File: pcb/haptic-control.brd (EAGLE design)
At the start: 40 x 160 mm, 47 parts, among them M1 SPH0641LM4H-1, U1 CC2642R, U2 SST26VF064B, U3 ICM20948, U4 74LVC1G17, U5 MCP1700T-1802TT, U6 PCA9306-DCU, U7 MTCH6301, X1 48MHz, X2 32.768kHz

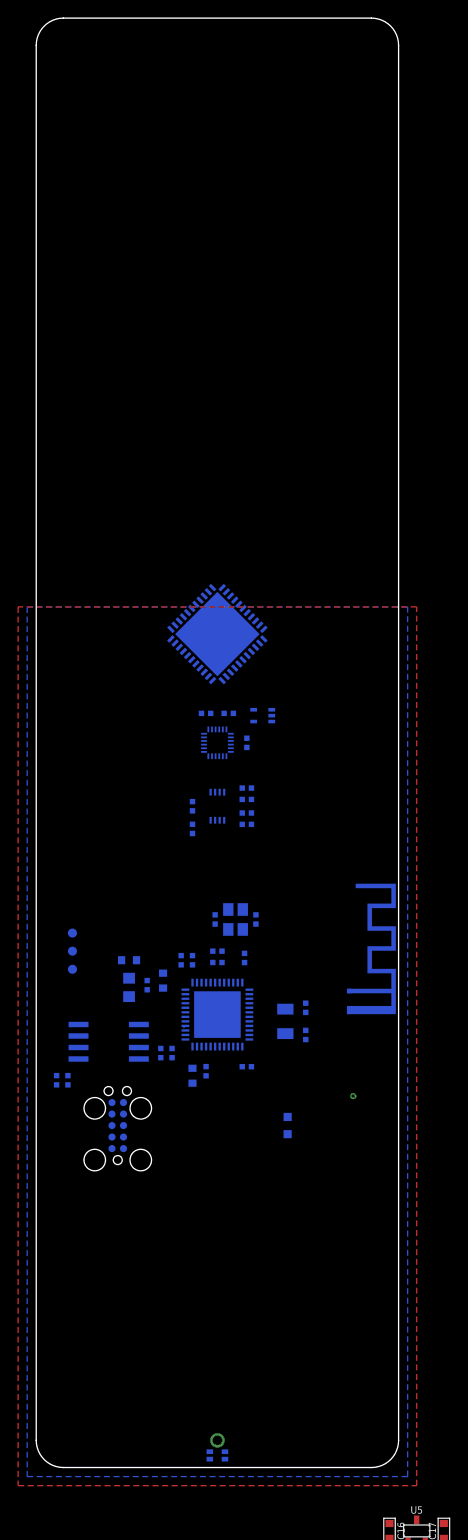
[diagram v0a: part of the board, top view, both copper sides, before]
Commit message: minor sch value modifications, and ic additions; minor pcb constraints changes
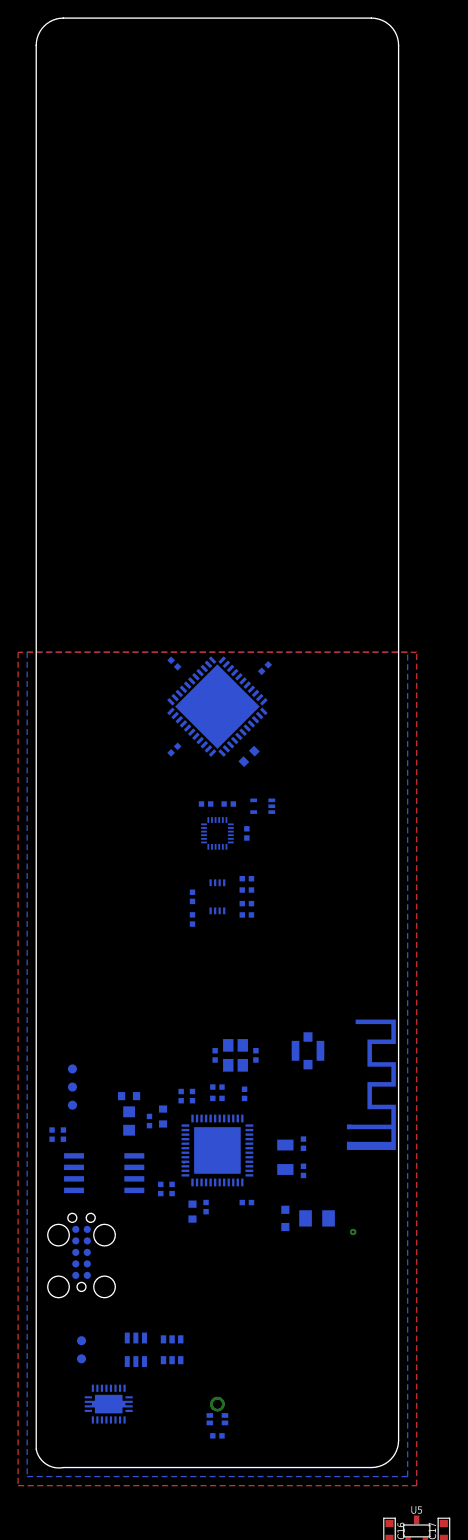
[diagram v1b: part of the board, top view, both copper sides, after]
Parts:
- added A1: U.FL, Connectors > Antennas:U.FL
- added C22, C23, C25, C26: 100n, Passive Components > Capacitors > Multilayer Ceramic Capacitors MLCC:_0402
- added C24: 10u, Passive Components > Capacitors > Multilayer Ceramic Capacitors MLCC:0603_WAVE
- added C27: 100u, Passive Components > Capacitors > Multilayer Ceramic Capacitors MLCC:_1206
- added TP4, TP5: TEST_POINT, Utility > Board:TEST_POINT
- added U$1: FS312F-G, Power > Battery Management:SOT23-6
- added U$2: FS8205, Semiconductors > Discrete Semiconductors > Transistors > MOSFETs:SOT23-6
- added U8: BQ51050B, Texas Instruments:VQFN20
- C10, C9: value 3p -> 12p
- C11, C12: value (none) -> np
- C4: value (none) -> 22u
- C6: value 10u -> 22u
- L1: value 10u -> 6u8
- L2: value filter -> BLM18HE152SN1
- moved C10 15.0 mm to (29.5, 35.8)
- moved C5 15.0 mm to (12.5, 38.2)
- moved C9 15.0 mm to (29.5, 32.8)
- moved C1 15.0 mm to (23.2, 29.2)
- moved C11 15.0 mm to (24.2, 45.5)
- moved C12 15.0 mm to (19.8, 45.5)
- moved C13 15.0 mm to (17.2, 28.2)
- moved C14 15.0 mm to (17.2, 41.0)
- moved C15 15.0 mm to (13.8, 30.8)
- moved C2 15.0 mm to (18.8, 28.8)
- moved C3 15.0 mm to (20.0, 40.8)
- moved C4 15.0 mm to (14.0, 38.8)
- moved C6 15.0 mm to (10.2, 41.0)
- moved C7 15.0 mm to (20.0, 42.0)
- moved C8 15.0 mm to (23.0, 41.2)
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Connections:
- new net N$10: C24.P$1, U7.7
- new net TC_!RESET: U7.18
- new net TC_INT: U7.8
- net 3.3V: now also C22.1, C23.1, C25.1, C26.1, C27.1, U7.17, U7.28, U7.40
- net GND: now also C22.2, C23.2, C24.P$2, C25.2, C26.2, C27.2, U7.16, U7.29, U7.39, U7.45, U7.6
- net SCL: now also U7.44
- net SDA: now also U7.1
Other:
- outline, holes or cut-outs redrawn

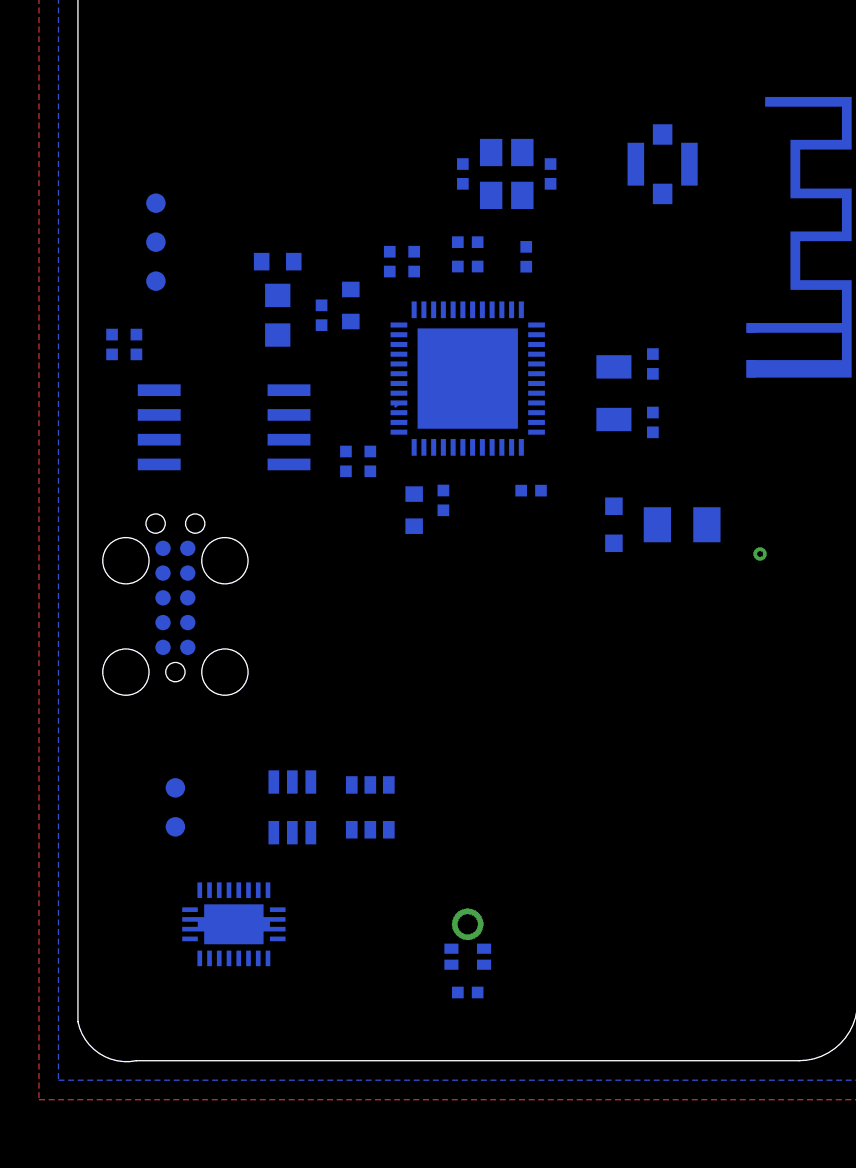
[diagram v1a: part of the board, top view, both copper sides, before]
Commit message: Hand merged previous commits: 	Added CC26x2 reference design 	Added antenna matching 	Connected labels to touch IC 	Added keepouts for the antenna 	Added more references/info to the board and schematic
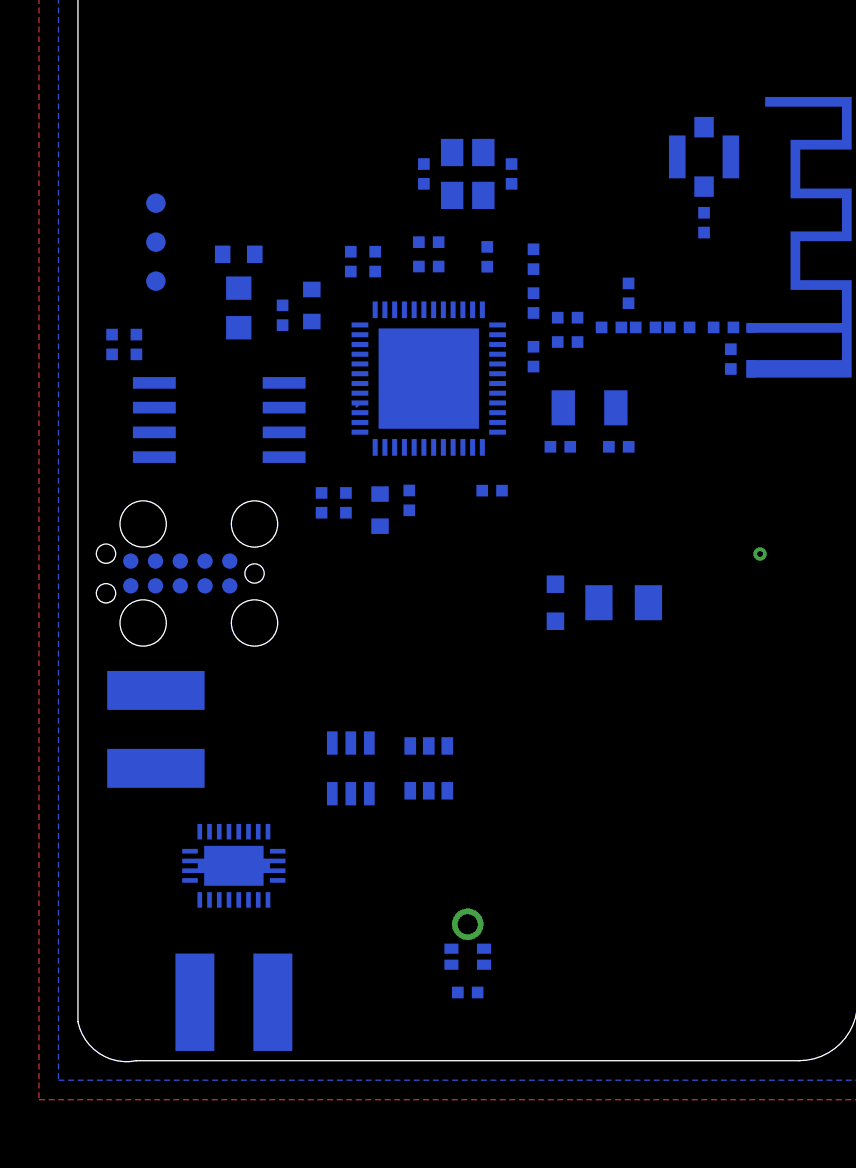
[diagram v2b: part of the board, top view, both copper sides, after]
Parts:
- removed TP4, TP5: TEST_POINT, Utility > Board:TEST_POINT
- added C28, C29, C31: 1p, Passive Components > Capacitors > Multilayer Ceramic Capacitors MLCC:_0402
- added C30, C33: 12p, Passive Components > Capacitors > Multilayer Ceramic Capacitors MLCC:_0402
- added C32: 1p8, Passive Components > Capacitors > Multilayer Ceramic Capacitors MLCC:_0402
- added C34, C35: DNP, Passive Components > Capacitors > Multilayer Ceramic Capacitors MLCC:_0402
- added L3, L4: 2n4, Passive Components > Inductors, Chokes & Coils:_0402
- added L5, L6: 2N, Passive Components > Inductors, Chokes & Coils:_0402
- added P1, P2: 2P-PAD, Generic Connector:PAD2X5MM-2P
- C11, C12: value np -> DNP
- moved C27 5.00 mm to (28.0, 23.5)
- moved L2 5.00 mm to (24.5, 23.5)
- moved C9 4.91 mm to (24.8, 31.5), turned to 0 degrees
- moved C10 4.60 mm to (27.8, 31.5), turned to 0 degrees
- moved U$1 3.61 mm to (14.0, 15.0)
- moved U$2 3.61 mm to (18.0, 15.0)
- moved U8 3.00 mm to (8.00, 10.0)
- moved C15 2.47 mm to (12.5, 28.6)
- moved R5 2.47 mm to (13.8, 28.6)
- moved A1 2.16 mm to (32.1, 46.4), turned to 270 degrees
- moved C6 2.03 mm to (8.25, 41.4)
- moved L1 2.03 mm to (8.25, 38.6)
- moved C1 2.00 mm to (21.2, 29.2)
- moved C11 2.00 mm to (22.2, 45.5)
- moved C12 2.00 mm to (17.8, 45.5)
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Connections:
- new net N$14: C30.1, L3.1
- new net N$15: C29.1, L4.1, L5.2
- new net N$16: C31.1, L5.1, L6.2
- new net N$17: C32.2, C35.1, E1.ANT
- new net N$18: C32.1, C33.2
- new net N$19: C33.1, C34.2, L6.1
- new net N$20: A1.P$3, C34.1
- new net PCAP_RX0: U7.27
- new net PCAP_RX1: U7.26
- new net PCAP_RX10: U7.14
- new net PCAP_RX11: U7.11
- new net PCAP_RX12: U7.10
- new net PCAP_RX2: U7.25
- new net PCAP_RX3: U7.24
- new net PCAP_RX4: U7.23
- new net PCAP_RX5: U7.22
- new net PCAP_RX6: U7.21
- new net PCAP_RX7: U7.20
- new net PCAP_RX8: U7.19
- new net PCAP_RX9: U7.15
- new net PCAP_TX0: U7.33
- new net PCAP_TX1: U7.32
- new net PCAP_TX10: U7.42
- new net PCAP_TX11: U7.43
- new net PCAP_TX12: U7.13
- new net PCAP_TX13: U7.12
- new net PCAP_TX14: U7.5
- new net PCAP_TX15: U7.4
- new net PCAP_TX16: U7.3
- new net PCAP_TX17: U7.2
- new net PCAP_TX2: U7.31
- new net PCAP_TX3: U7.30
- new net PCAP_TX4: U7.34
- new net PCAP_TX5: U7.38
- new net PCAP_TX6: U7.37
- new net PCAP_TX7: U7.36
- new net PCAP_TX8: U7.35
- new net PCAP_TX9: U7.41
- net GND: now also A1.P$1, A1.P$2, C28.1, C30.2, C31.2, C35.2, E1.GND
- net N$1: now also C28.2, L4.2
- net N$3: now also C29.2, L3.2

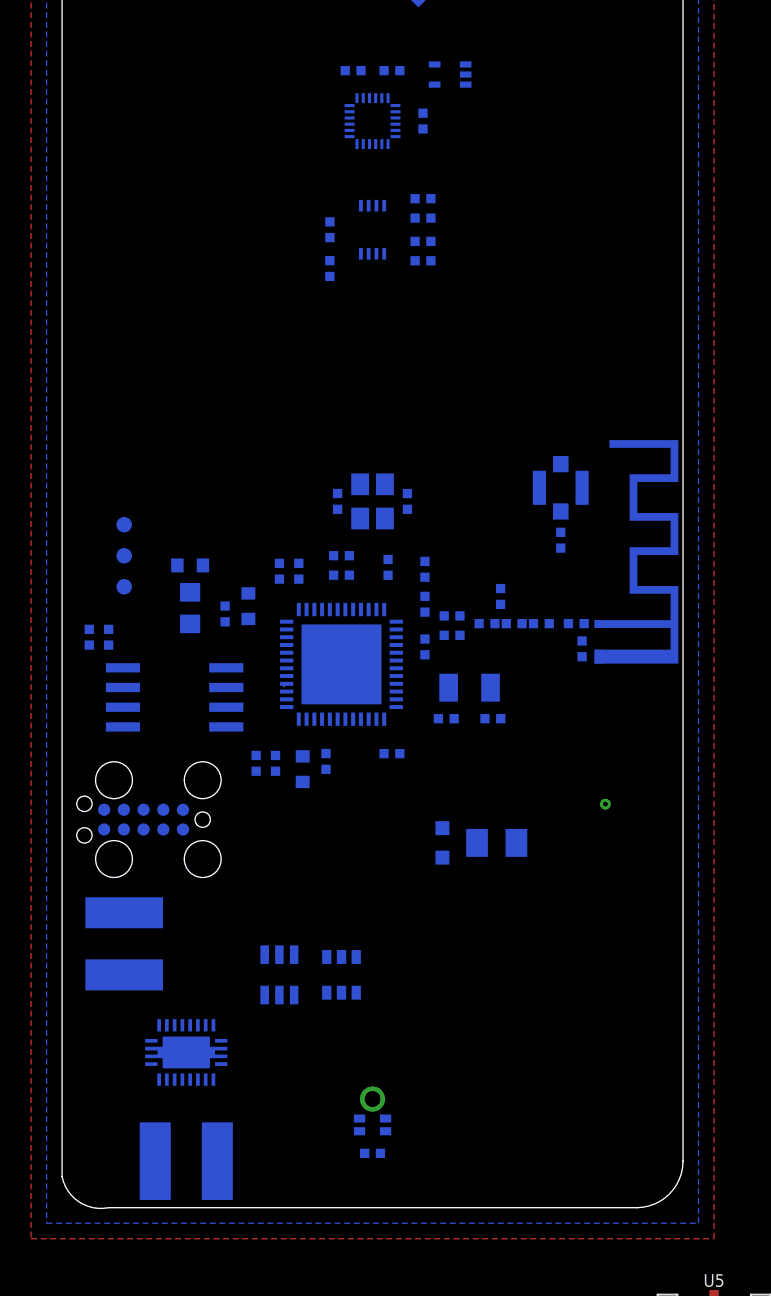
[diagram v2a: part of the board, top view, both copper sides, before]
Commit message: added battery and coil pads, changed mcu orientation
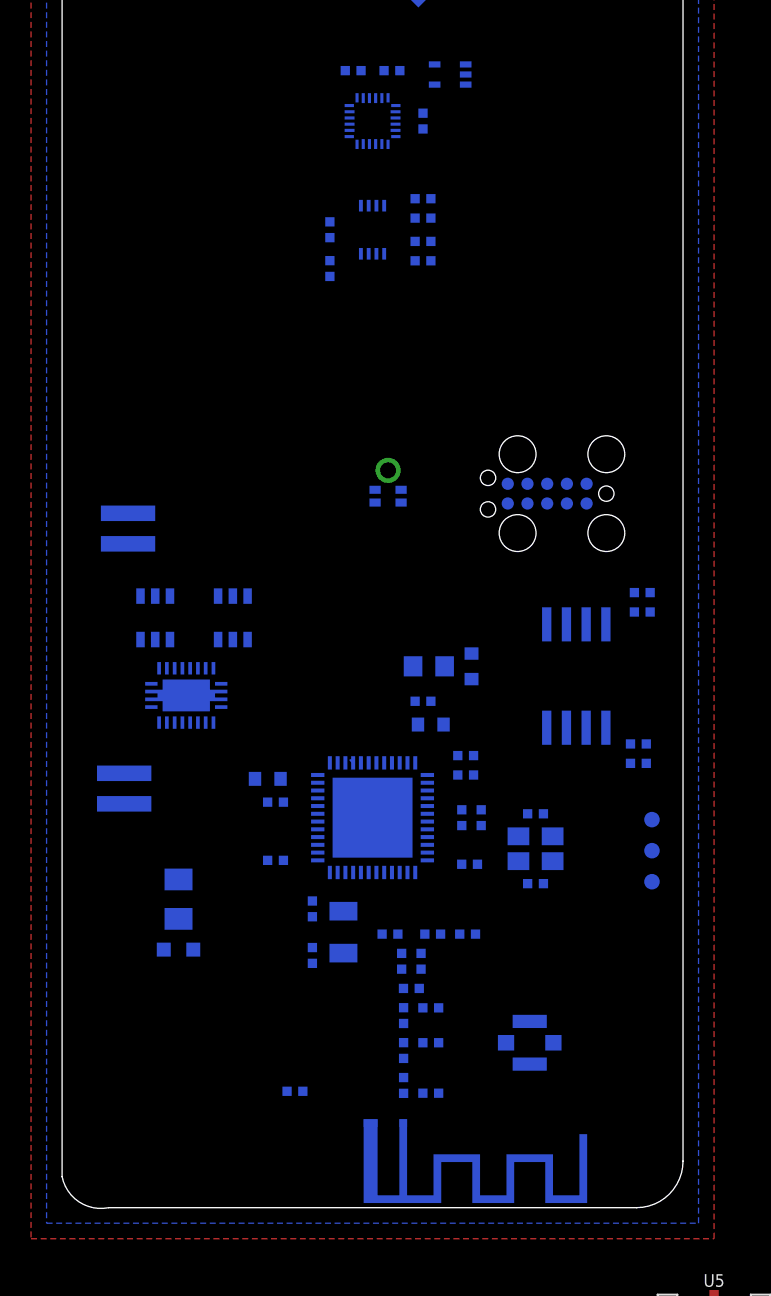
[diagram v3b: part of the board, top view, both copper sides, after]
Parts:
- removed P1, P2: 2P-PAD, Generic Connector:PAD2X5MM-2P
- removed U$1: FS312F-G, Power > Battery Management:SOT23-6
- removed U$2: FS8205, Semiconductors > Discrete Semiconductors > Transistors > MOSFETs:SOT23-6
- added J1, J2: PAD1X3_5MM-2P, Connectors > Other:PAD1X3_5MM-2P
- added U10: FS8205, Fortune:SOT23-6
- added U9: FS312F-G, Fortune:SOT23-6
- moved TP1 41.0 mm to (38.0, 21.0), turned to 180 degrees
- moved M1 40.5 mm to (21.0, 47.5)
- moved TP2 38.9 mm to (38.0, 23.0), turned to 180 degrees
- moved TP3 37.2 mm to (38.0, 25.0), turned to 180 degrees
- moved R2 36.0 mm to (37.1, 29.9), turned to 180 degrees
- moved A1 35.8 mm to (30.1, 10.6), turned to 0 degrees
- moved R4 35.1 mm to (37.1, 28.6), turned to 180 degrees
- moved E1 34.8 mm to (22.0, 5.20), turned to 180 degrees
- moved C34 33.4 mm to (23.8, 10.6), turned to 0 degrees
- moved TC1 33.4 mm to (31.2, 46.0)
- moved C32 31.8 mm to (22.0, 7.88), turned to 270 degrees
- moved C35 30.2 mm to (23.8, 7.38), turned to 180 degrees
- moved C33 28.9 mm to (22.0, 10.1), turned to 270 degrees
- moved C31 26.9 mm to (23.8, 12.9), turned to 180 degrees
- moved C15 26.7 mm to (37.4, 38.4), turned to 0 degrees
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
